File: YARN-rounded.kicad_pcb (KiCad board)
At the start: 2 copper layers, 99 x 91.7 mm, 16 parts, among them J1 Cart System Out, J2 Cart Main In, J3 Cart Exp In, SW1 SW_SPDT, SW2 SW_SPDT, SW3 SW_DPDT_x2, U1 74HC541, U2 74HC541, U3 74HC541

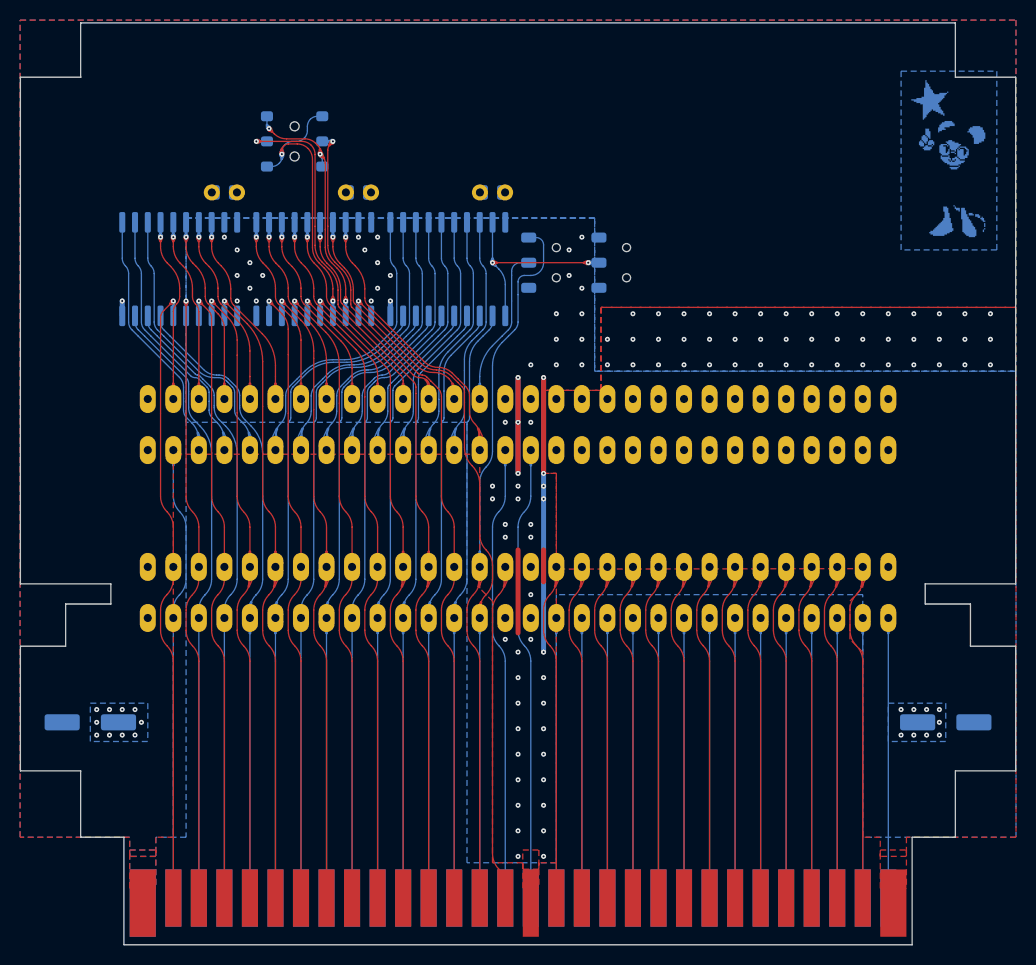
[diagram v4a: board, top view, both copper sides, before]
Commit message: Redesign decoding architecture
Thanks, lidnariq and Perkka!
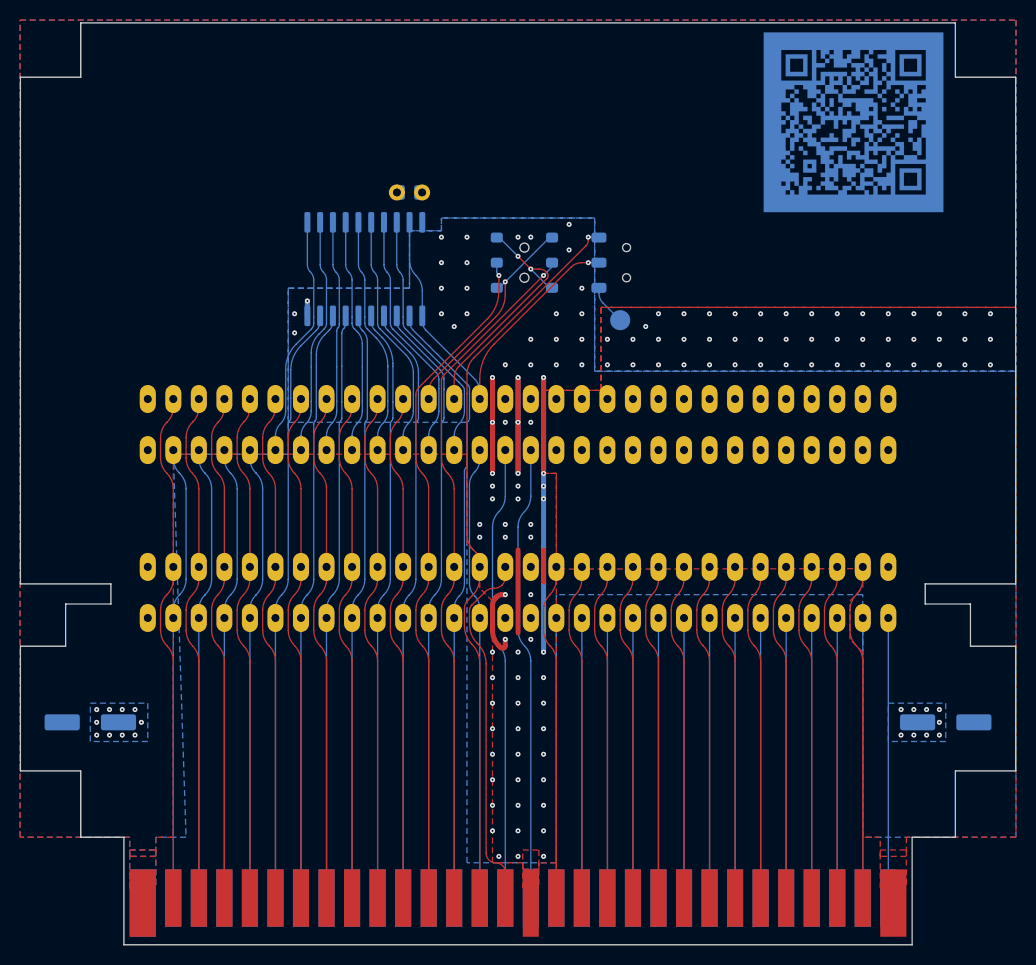
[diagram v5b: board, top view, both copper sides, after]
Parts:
- removed C2, C3: 0.1uF, YARN:C_Disc-0805_D3.0mm_W1.6mm_P2.50mm
- removed LOGO-1: dagga_star_yoeynsf, YARN:dagga_star_yoeynsf
- removed the SW2 at (130.8, 69.8)
- removed U2, U3: 74HC541, Package_SO:SOIC-20W_7.5x12.8mm_P1.27mm
- added TP1: EXP_~{CE}, TestPoint:TestPoint_Pad_D2.0mm, B.Cu at (137.2, 75.6)
- moved SW2 25.8 mm to (127.6, 69.8)
- moved C1 8.25 mm to (116.2, 62.9)
- moved U1 8.25 mm to (111.8, 70.5)
- moved LOGO-2 3.18 mm to (147.3, 55.9)
- renumbered SW3 to SW2
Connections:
- J3 pad 10: /S_CPU_A3 -> /CPU_A3
- J3 pad 11: /S_CPU_A2 -> /CPU_A2
- J3 pad 12: /S_CPU_A1 -> /CPU_A1_V
- J3 pad 13: /S_CPU_A0 -> /CPU_A0_V
- J3 pad 2: /S_CPU_A11 -> /CPU_A11
- J3 pad 3: /S_CPU_A10 -> /CPU_A10
- J3 pad 33: /S_CPU_A12 -> /CPU_A12
- J3 pad 34: /S_CPU_A13 -> /CPU_A13
- J3 pad 35: /S_CPU_A14 -> /CPU_A14
- J3 pad 4: /S_CPU_A9 -> /CPU_A9
- J3 pad 44: /S_~{ROMSEL} -> /~{ROMSEL}
- J3 pad 5: /S_CPU_A8 -> /CPU_A8
- J3 pad 56: VCC -> GND
- J3 pad 6: /S_CPU_A7 -> /CPU_A7
- J3 pad 7: /S_CPU_A6 -> /CPU_A6
- J3 pad 8: /S_CPU_A5 -> /CPU_A5
- J3 pad 9: /S_CPU_A4 -> /CPU_A4
- SW1 pad 1: GND -> /CPU_R~{W}
- SW1 pad 2: /S_~{CE} -> /S_CPU_R~{W}
- SW1 pad 3: VCC -> Net-(SW1-C)
- U1 pad 1: /S_~{CE} -> /S_CPU_R~{W}
- U1 pad 19: /S_~{CE} -> /S_CPU_R~{W}
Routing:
- net /S_~{ROMSEL}: track 28.4 -> 0.00 mm, vias 1 -> 0
- net /S_CPU_A14: track 27.4 -> 0.00 mm
- net /S_CPU_A13: track 26.2 -> 0.00 mm
- net /S_CPU_A12: track 25.4 -> 0.00 mm
- net GND: track 70.3 -> 95.4 mm, vias 76 -> 89
- net /S_CPU_R~{W}: track 15.9 -> 39.6 mm, vias 0 -> 1
- net /S_CPU_A0: track 23.1 -> 0.00 mm, vias 1 -> 0
- net /S_CPU_A1: track 22.1 -> 0.00 mm, vias 1 -> 0
- net /~{ROMSEL}: track 67.1 -> 45.1 mm, vias 1 -> 0
- net /S_CPU_A2: track 21.2 -> 0.00 mm, vias 1 -> 0
- net /S_CPU_A3: track 20.6 -> 0.00 mm, vias 1 -> 0
- net /S_~{CE}: track 20.3 -> 0.00 mm, vias 2 -> 0
- net /S_CPU_A4: track 20.0 -> 0.00 mm, vias 1 -> 0
- net /S_CPU_A7: track 19.7 -> 0.00 mm, vias 1 -> 0
- net /S_CPU_A5: track 19.4 -> 0.00 mm, vias 1 -> 0
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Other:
- board text added: "VRC6B NORMAL"
- board text added: "~{W} PASS TP PASS"
- board text removed: "Dx PASS Dx Z"
- board text removed: "R~{W} PASS ~{W}"
- board text removed: "VRC6B VRC6A"
